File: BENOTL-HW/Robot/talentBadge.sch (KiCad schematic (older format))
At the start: 62 parts, among them P1 USB_A, P2 OLED, P3 Batt, P4 PS, P5 sd_card_spi, Q1 MMBT3904, Q2 MMBT3904, Q3 IR phototransistor, SW1 B1, SW2 B2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

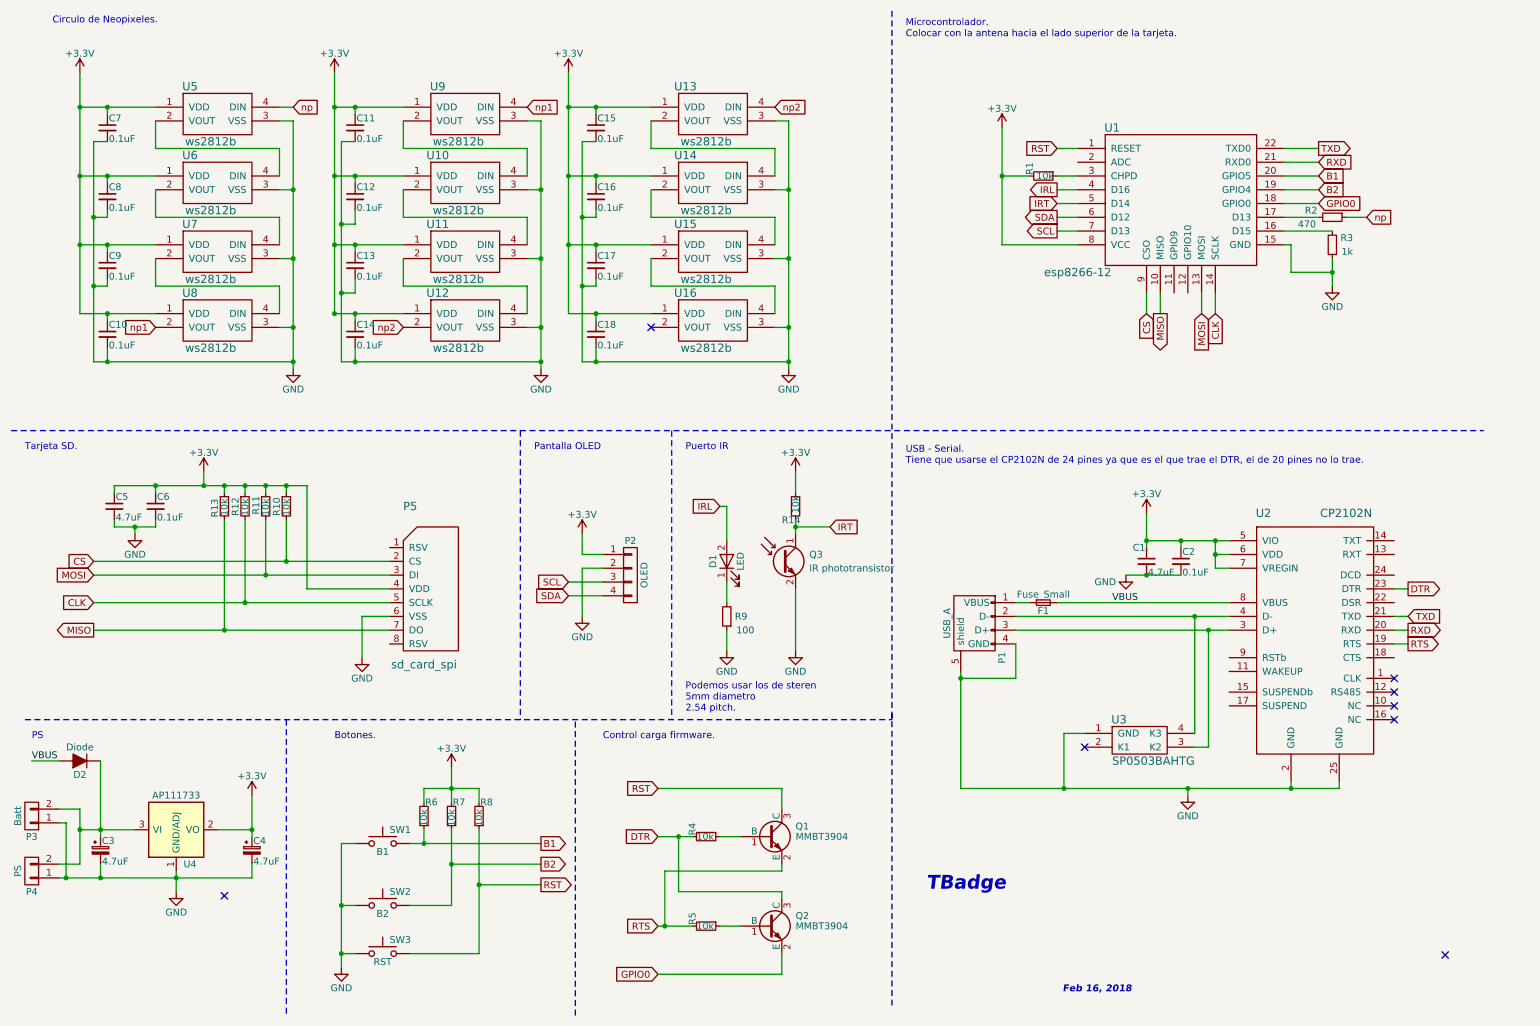
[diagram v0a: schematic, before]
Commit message: Update schematic robot
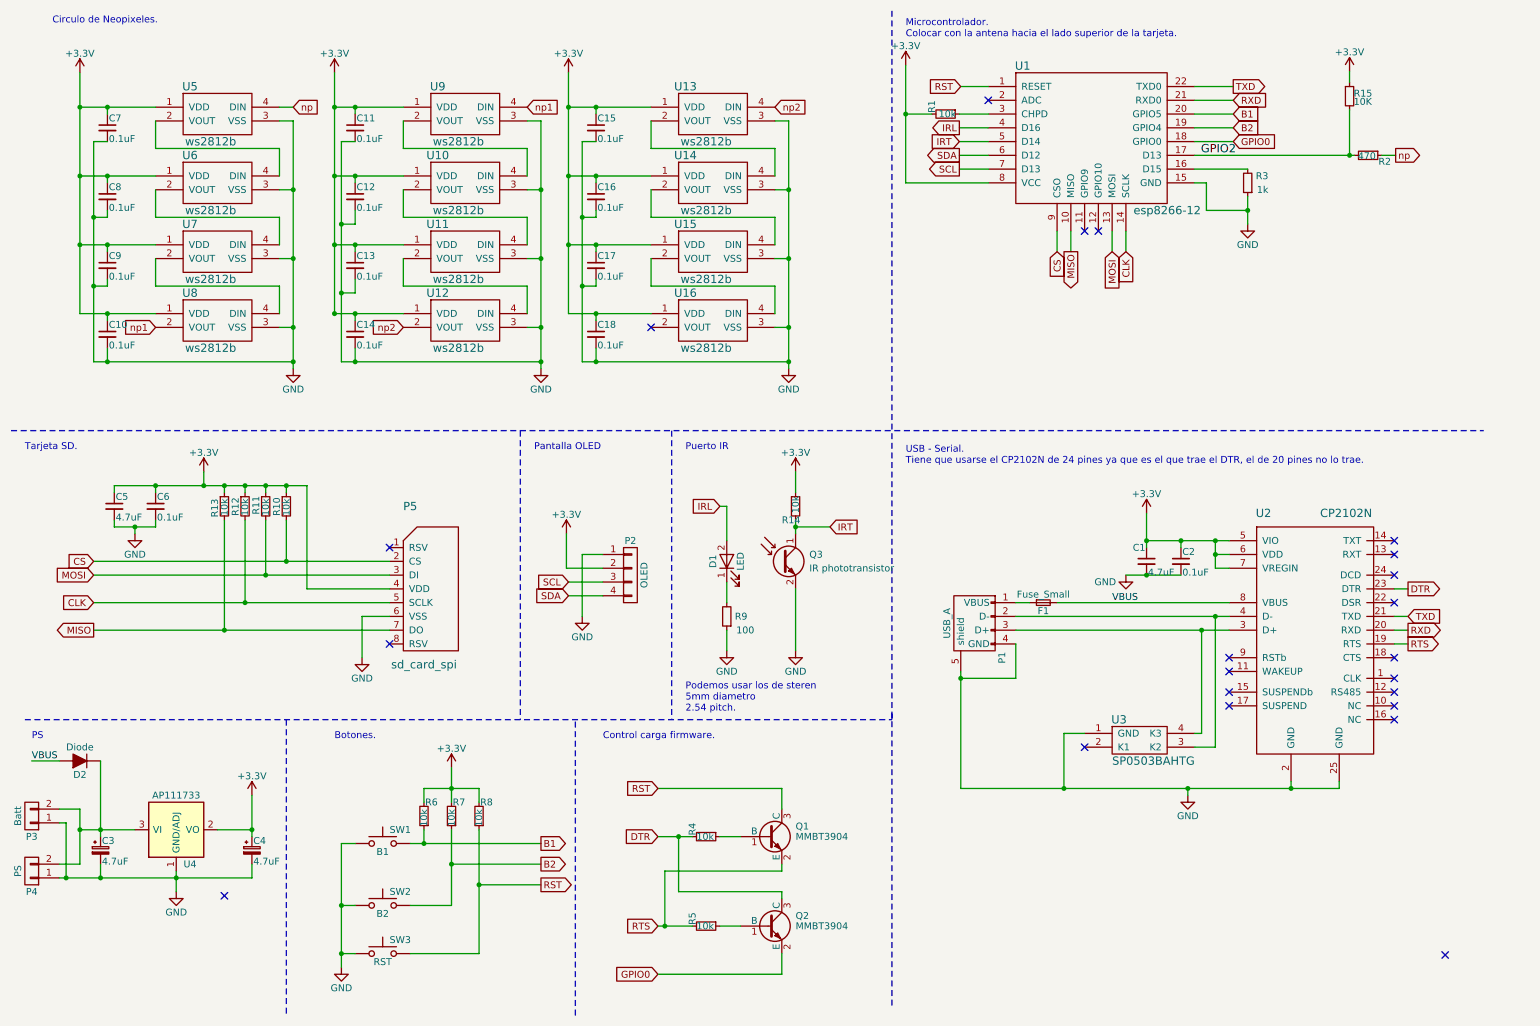
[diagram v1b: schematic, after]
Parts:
- added R15: 10K, Resistors_SMD:R_0805_HandSoldering, symbol R_Small
- U1: footprint talentBadge:ESP-12E_SMD -> ESP8266:ESP-12E
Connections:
- net +3V3: now also P2.2 (P2), R15.1; no longer P2.1 (P1)
- net GND: now also P2.1 (P1); no longer P2.2 (P2)
- net at P1.3 (D+), U2.3 (D+): now also U3.4 (K3); no longer U3.3 (K2)
- net at P1.2 (D-), U2.4 (D-): now also U3.3 (K2); no longer U3.4 (K3)
- net GPIO2: now reaches R2.2, U1.17 (D13)
- net GPIO2: now also R15.2
- no-connect marks 8 -> 22
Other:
- note removed: "Feb 16, 2018\n"
- note removed: "TBadge"
- moved on the sheet: R1, R2, R3

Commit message: Change footprint ESP8266
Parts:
- U1: footprint ESP8266:ESP-12E -> RF_Modules:ESP-12E
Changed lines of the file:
@@
 F 0 "U1" H 7850 2900 60  0000 C CNN
 F 1 "esp8266-12" H 8900 1850 60  0000 C CNN
-F 2 "ESP8266:ESP-12E" H 7800 2050 60  0001 C CNN
+F 2 "RF_Modules:ESP-12E" H 7800 2050 60  0001 C CNN
 F 3 "" H 7800 2050 60  0000 C CNN
 	1    8350 1900

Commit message: Update C4, C3 y C5
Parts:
- C3, C4: footprint Capacitors_SMD:C_0805_HandSoldering -> Capacitors_Tantalum_SMD:CP_Tantalum_Case-A_EIA-3216-18_Hand
- C5: PartNo TPSA475K010T1400 -> 885012107013
- U1: footprint RF_Modules:ESP-12E -> talentBadge:esp8266-12
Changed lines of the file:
@@
 F 0 "C3" H 1160 6670 50  0000 L CNN
 F 1 "4.7uF" H 1160 6520 50  0000 L CNN
-F 2 "Capacitors_SMD:C_0805_HandSoldering" H 1150 6600 50  0001 C CNN
+F 2 "Capacitors_Tantalum_SMD:CP_Tantalum_Case-A_EIA-3216-18_Hand" H 1150 6600 50  0001 C CNN
 F 3 "https://www.mouser.com/ds/2/40/TPS_AUTO-845414.pdf" H 1150 6600 50  0001 C CNN
 F 4 "TPSA475K010T1400" H 1150 6600 60  0001 C CNN "PartNo"
@@
 F 2 "Capacitors_SMD:C_0805_HandSoldering" H 1250 4100 50  0001 C CNN
 F 3 "https://www.mouser.com/ds/2/40/TPS_AUTO-845414.pdf" H 1250 4100 50  0001 C CNN
-F 4 "TPSA475K010T1400 " H 1250 4100 60  0001 C CNN "PartNo"
+F 4 "885012107013" H 1250 4100 60  0001 C CNN "PartNo"
 	1    1250 4100
 	1    0    0    -1
@@
 F 0 "C4" H 2260 6670 50  0000 L CNN
 F 1 "4.7uF" H 2260 6520 50  0000 L CNN
-F 2 "Capacitors_SMD:C_0805_HandSoldering" H 2250 6600 50  0001 C CNN
+F 2 "Capacitors_Tantalum_SMD:CP_Tantalum_Case-A_EIA-3216-18_Hand" H 2250 6600 50  0001 C CNN
 F 3 "https://www.mouser.com/ds/2/40/TPS_AUTO-845414.pdf" H 2250 6600 50  0001 C CNN
 F 4 "TPSA475K010T1400" H 2250 6600 60  0001 C CNN "PartNo"
@@
 F 0 "U1" H 7850 2900 60  0000 C CNN
 F 1 "esp8266-12" H 8900 1850 60  0000 C CNN
-F 2 "RF_Modules:ESP-12E" H 7800 2050 60  0001 C CNN
+F 2 "talentBadge:esp8266-12" H 7800 2050 60  0001 C CNN
 F 3 "" H 7800 2050 60  0000 C CNN
 	1    8350 1900

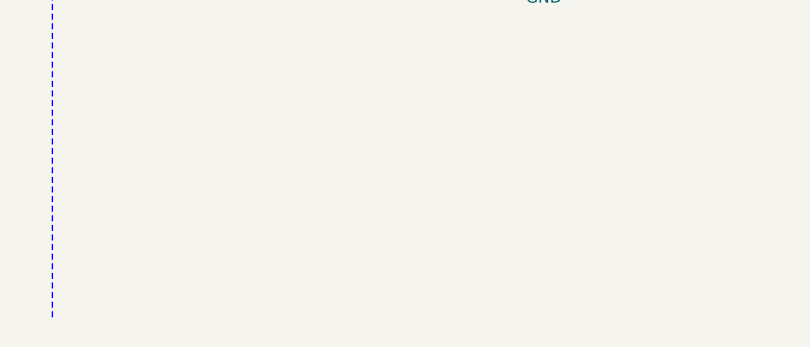
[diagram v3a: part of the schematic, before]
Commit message: R3 y R2 agregado al BOM
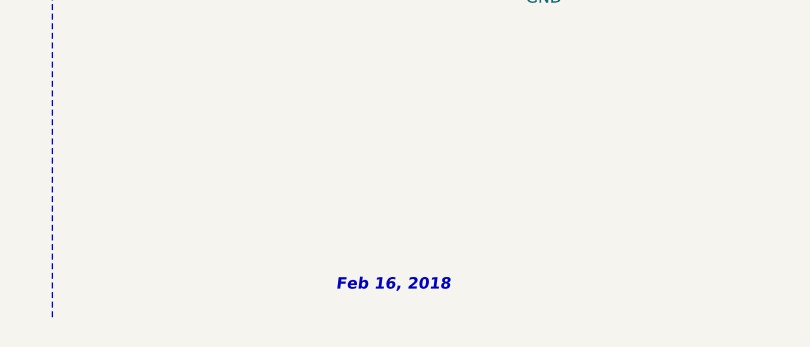
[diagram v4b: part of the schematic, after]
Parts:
- C3, C4: footprint Capacitors_Tantalum_SMD:CP_Tantalum_Case-A_EIA-3216-18_Hand -> Capacitors_SMD:C_0805_HandSoldering
- C5: PartNo 885012107013 -> TPSA475K010T1400
- R2: PartNo (none) -> CR0805-FX-4700ELF
- R3: PartNo (none) -> RC0805JR-071KL
- U1: footprint talentBadge:esp8266-12 -> (none)
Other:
- note added: "Feb 16, 2018\n"
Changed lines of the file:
@@
 Sheet 1 1
 Title "The badge of the Lands"
-Date "2018-02-16"
-Rev "0.2"
+Date "2018-03-07"
+Rev "0.3"
 Comp "Unofficial Badge of Talent Land 2018"
 Comment1 "Andres Sabas"
-Comment2 ""
-Comment3 ""
-Comment4 ""
+Comment2 "Eden Candelas"
+Comment3 "Eduardo Contreras"
+Comment4 "Gustavo Reynaga"
 $EndDescr
 $Comp
@@
 F 0 "C3" H 1160 6670 50  0000 L CNN
 F 1 "4.7uF" H 1160 6520 50  0000 L CNN
-F 2 "Capacitors_Tantalum_SMD:CP_Tantalum_Case-A_EIA-3216-18_Hand" H 1150 6600 50  0001 C CNN
+F 2 "Capacitors_SMD:C_0805_HandSoldering" H 1150 6600 50  0001 C CNN
 F 3 "https://www.mouser.com/ds/2/40/TPS_AUTO-845414.pdf" H 1150 6600 50  0001 C CNN
 F 4 "TPSA475K010T1400" H 1150 6600 60  0001 C CNN "PartNo"
@@
 F 2 "Resistors_SMD:R_0805_HandSoldering" H 10360 1550 50  0001 C CNN
 F 3 "" H 10360 1550 50  0000 C CNN
+F 4 "CR0805-FX-4700ELF" V 10360 1550 60  0001 C CNN "PartNo"
 	1    10360 1550
 	0    1    1    0
@@
 F 2 "Capacitors_SMD:C_0805_HandSoldering" H 1250 4100 50  0001 C CNN
 F 3 "https://www.mouser.com/ds/2/40/TPS_AUTO-845414.pdf" H 1250 4100 50  0001 C CNN
-F 4 "885012107013" H 1250 4100 60  0001 C CNN "PartNo"
+F 4 "TPSA475K010T1400 " H 1250 4100 60  0001 C CNN "PartNo"
 	1    1250 4100
 	1    0    0    -1
@@
 	1    0    0    -1
 $EndComp
+Text Notes 8140 7640 0    50   Italic 10
+Feb 16, 2018\n
 Text GLabel 8100 2250 3    50   Input ~ 0
 CS
@@
 F 2 "Resistors_SMD:R_0805_HandSoldering" H 9485 1750 50  0001 C CNN
 F 3 "" H 9485 1750 50  0000 C CNN
+F 4 "RC0805JR-071KL" H 9485 1750 60  0001 C CNN "PartNo"
 	1    9485 1750
 	-1   0    0    1
@@
 IRL
 $Comp
-L GND #PWR021
+L GND #PWR022
 U 1 1 5A914774
 P 6200 5150
-F 0 "#PWR021" H 6200 4900 50  0001 C CNN
+F 0 "#PWR022" H 6200 4900 50  0001 C CNN
 F 1 "GND" H 6200 5000 50  0000 C CNN
 F 2 "" H 6200 5150 50  0000 C CNN
@@
 $EndComp
 $Comp
-L +3.3V #PWR022
+L +3.3V #PWR023
 U 1 1 5A916FB2
 P 6200 3850
-F 0 "#PWR022" H 6200 3700 50  0001 C CNN
+F 0 "#PWR023" H 6200 3700 50  0001 C CNN
 F 1 "+3.3V" H 6200 3990 50  0000 C CNN
 F 2 "" H 6200 3850 50  0000 C CNN
@@
 F 0 "C4" H 2260 6670 50  0000 L CNN
 F 1 "4.7uF" H 2260 6520 50  0000 L CNN
-F 2 "Capacitors_Tantalum_SMD:CP_Tantalum_Case-A_EIA-3216-18_Hand" H 2250 6600 50  0001 C CNN
+F 2 "Capacitors_SMD:C_0805_HandSoldering" H 2250 6600 50  0001 C CNN
 F 3 "https://www.mouser.com/ds/2/40/TPS_AUTO-845414.pdf" H 2250 6600 50  0001 C CNN
 F 4 "TPSA475K010T1400" H 2250 6600 60  0001 C CNN "PartNo"
@@
 $EndComp
 $Comp
-L +3.3V #PWR023
+L +3.3V #PWR024
 U 1 1 5A8CED38
 P 10225 940
-F 0 "#PWR023" H 10225 790 50  0001 C CNN
+F 0 "#PWR024" H 10225 790 50  0001 C CNN
 F 1 "+3.3V" H 10225 1080 50  0000 C CNN
 F 2 "" H 10225 940 50  0000 C CNN
@@
 F 0 "U1" H 7850 2900 60  0000 C CNN
 F 1 "esp8266-12" H 8900 1850 60  0000 C CNN
-F 2 "talentBadge:esp8266-12" H 7800 2050 60  0001 C CNN
+F 2 "" H 7800 2050 60  0000 C CNN
 F 3 "" H 7800 2050 60  0000 C CNN
 	1    8350 1900
@@
 NoConn ~ 10550 4800
 $Comp
-L GND #PWR024
+L GND #PWR021
 U 1 1 5A9146B5
 P 5700 5150
-F 0 "#PWR024" H 5700 4900 50  0001 C CNN
+F 0 "#PWR021" H 5700 4900 50  0001 C CNN
 F 1 "GND" H 5700 5000 50  0000 C CNN
 F 2 "" H 5700 5150 50  0000 C CNN

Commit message: Vinculado footprint ESP-WROOM-02
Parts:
- removed U1: esp8266-12, symbol esp8266-12
- added U1: ESP-13-WROOM-02, talentBadge:ESP-13-WROOM-02, symbol ESP-13-WROOM-02
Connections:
- net labels removed: GPIO2
- wire segments 231 -> 235
- no-connect marks 22 -> 20
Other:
- note removed: "Feb 16, 2018\n"
- moved on the sheet: R1, R15, R2, R3
